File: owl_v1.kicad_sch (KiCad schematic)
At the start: 14 parts, among them SW1 SW_SPDT, U1 STM32F103C8T6, Y1 8MHz, Y2 32k768

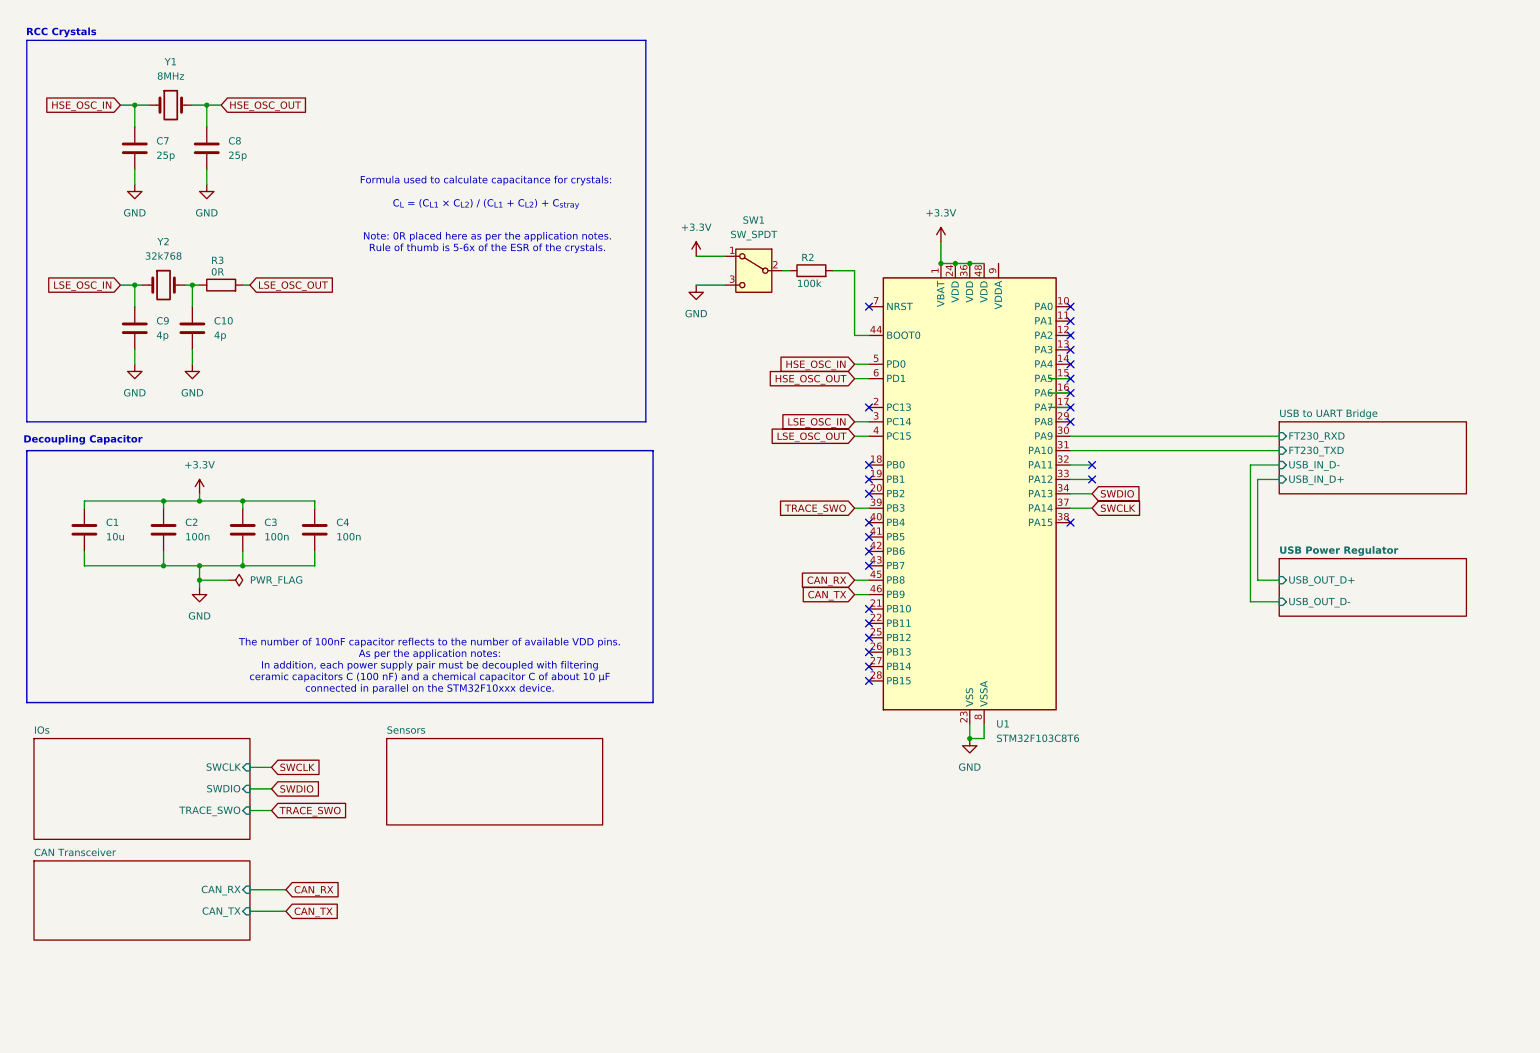
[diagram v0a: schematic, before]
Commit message: [feat] Add breakout for SPI1 for IMU
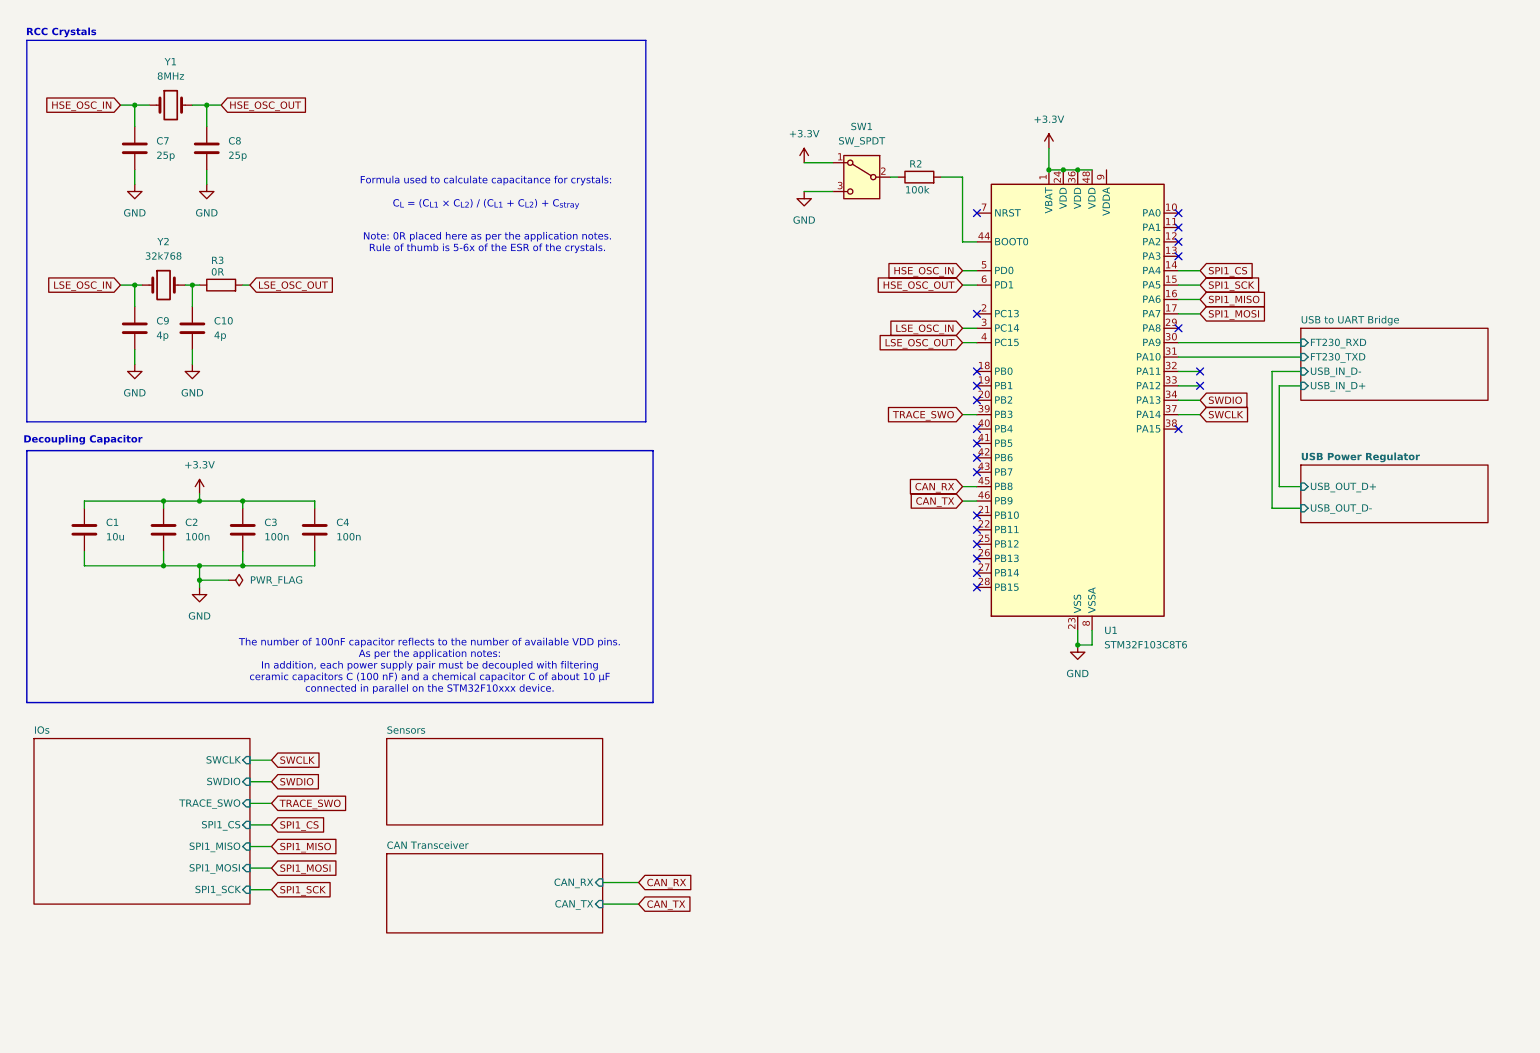
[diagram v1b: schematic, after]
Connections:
- net SPI1_CS: now reaches U1.14 (PA4)
- net SPI1_SCK: now reaches U1.15 (PA5)
- net SPI1_MISO: now reaches U1.16 (PA6)
- net SPI1_MOSI: now reaches U1.17 (PA7)
- no-connect marks 27 -> 23
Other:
- sheet IOs ports: added SPI1_CS, SPI1_MISO, SPI1_MOSI, SPI1_SCK; removed none
- moved on the sheet: R2, SW1, U1

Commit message: [feat] Add analogue filter
The analogue filter has been copied from Phil's lab SimpleTM32
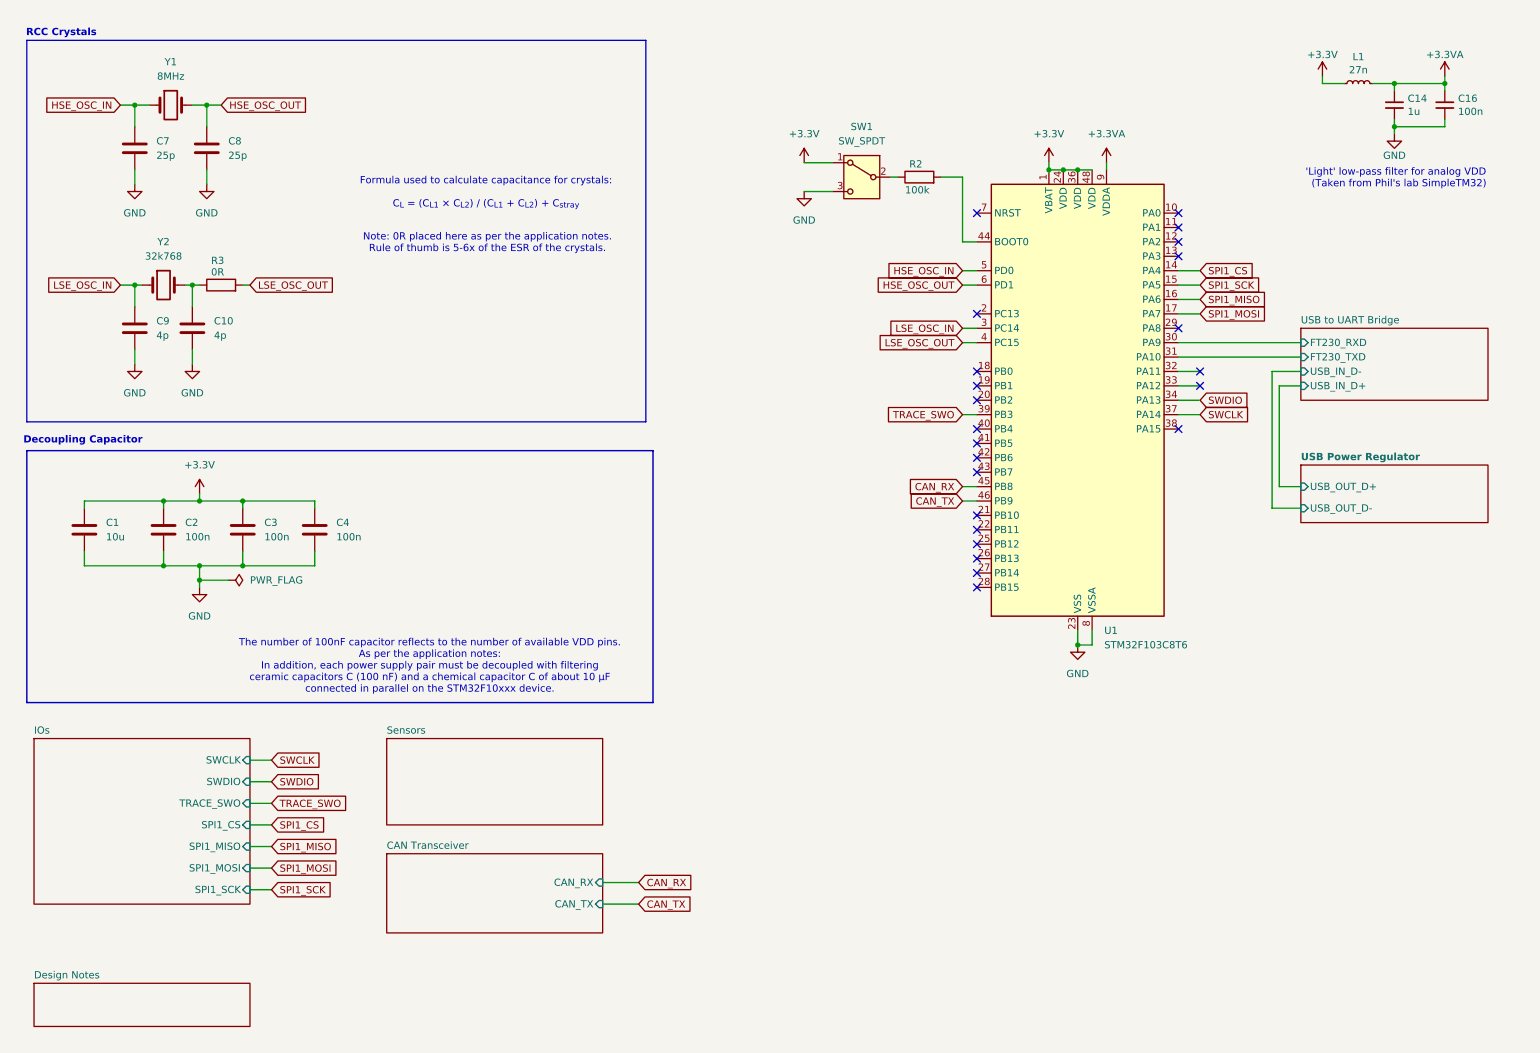
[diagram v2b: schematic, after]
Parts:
- added C14: 1u, Capacitor_SMD:C_0402_1005Metric, symbol Device:C_Small
- added C16: 100n, Capacitor_SMD:C_0402_1005Metric, symbol Device:C_Small
- added L1: 27n, Inductor_SMD:L_0402_1005Metric, symbol Device:L_Small
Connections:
- net +3.3V: now also L1.1
- net GND: now also C14.2, C16.2
- net +3.3VA: now reaches U1.9 (VDDA)
- net +3.3VA: now also C14.1, C16.1, L1.2
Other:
- added sheet Design Notes (design_notes.kicad_sch)
- note added: "'Light' low-pass filter for analog VDD (Taken from Phil's lab SimpleTM32)"

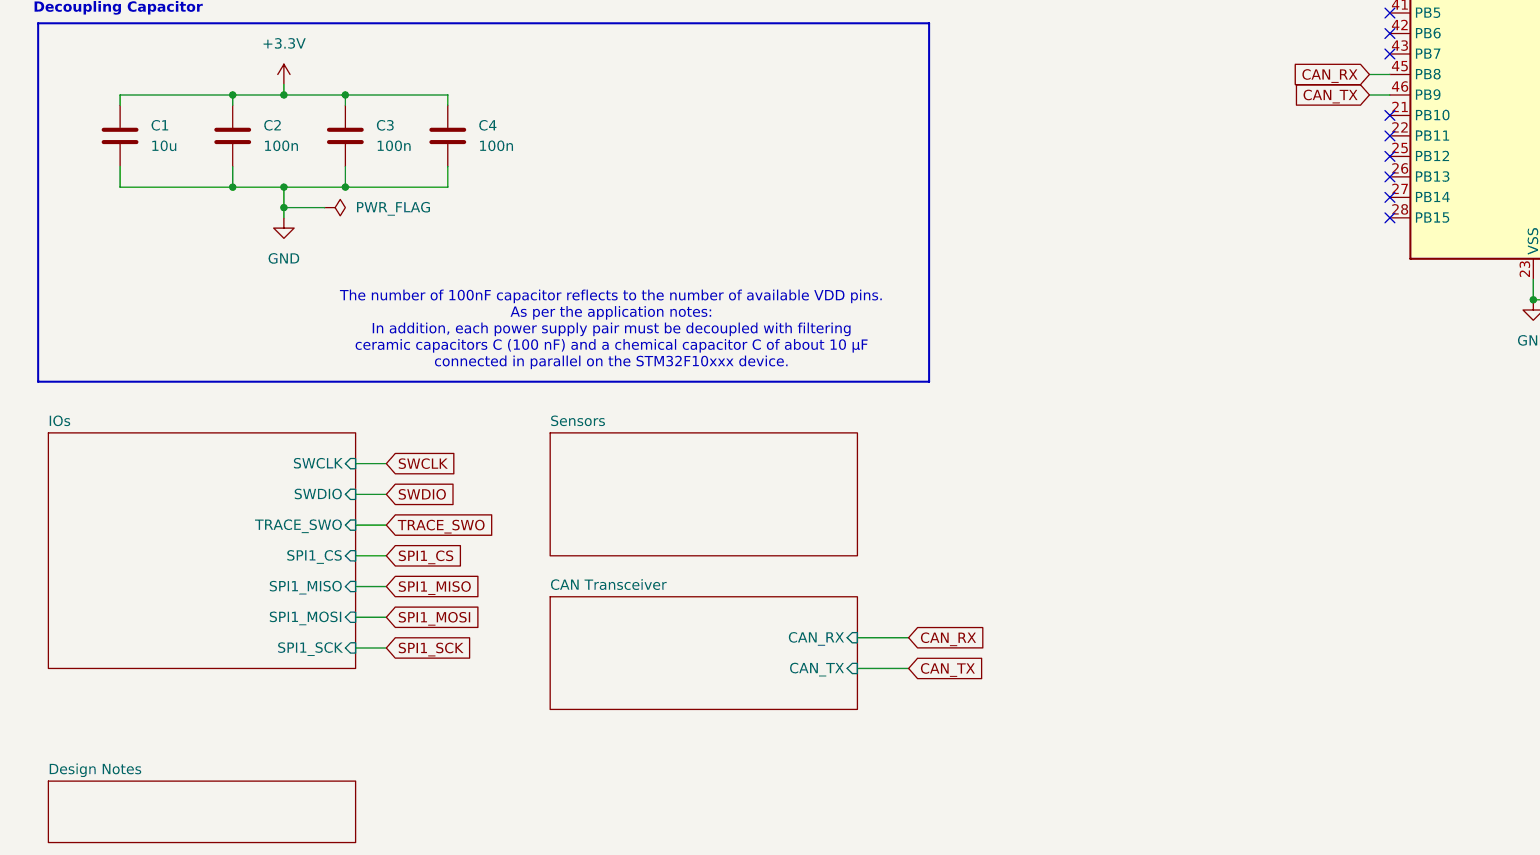
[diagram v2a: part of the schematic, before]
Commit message: [feat] Integrate MicroSD Card into the board with SPI2
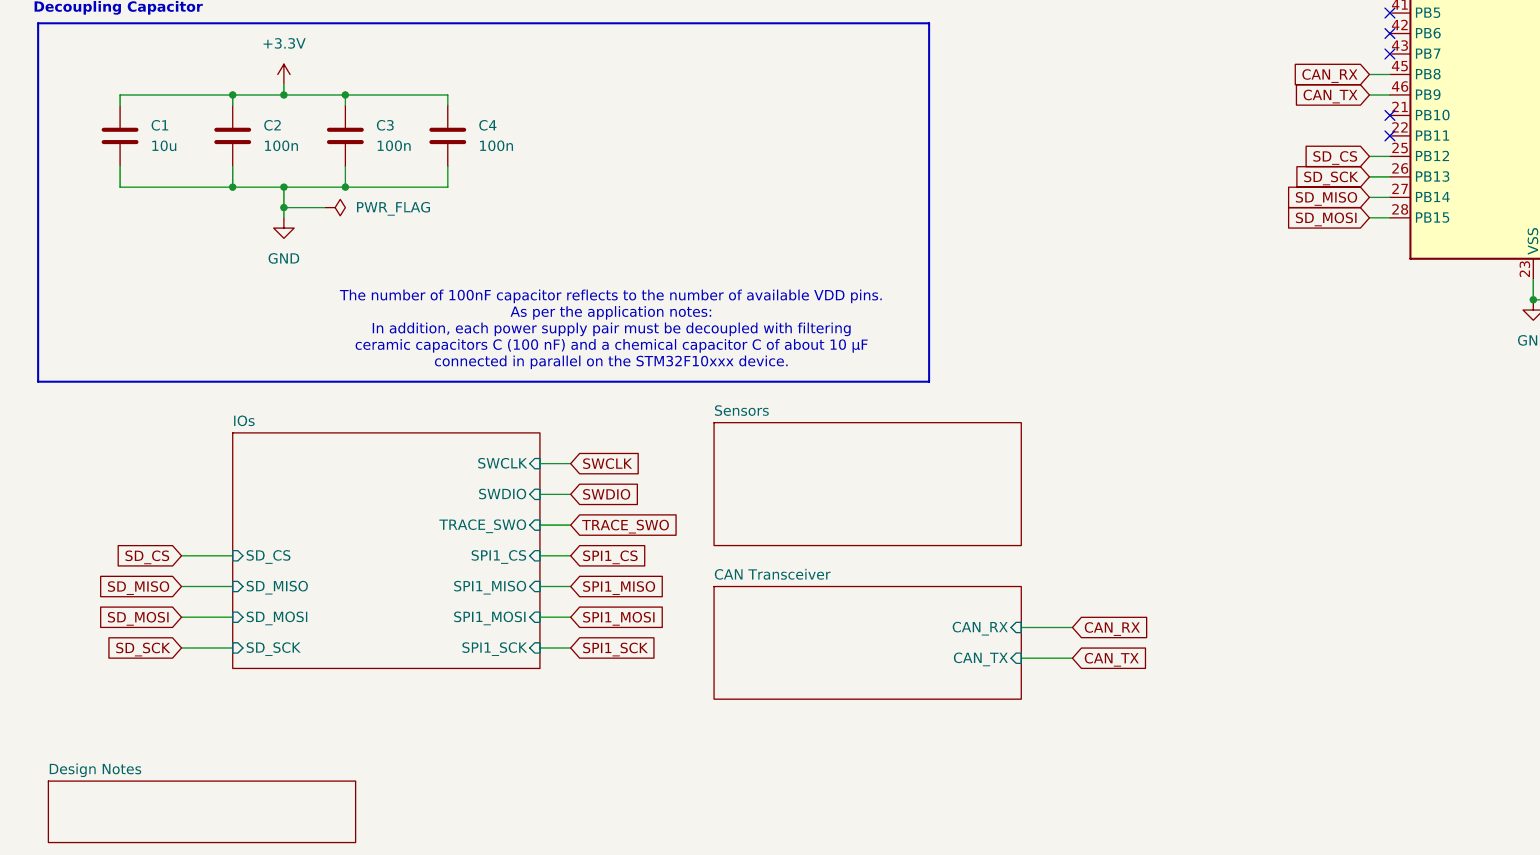
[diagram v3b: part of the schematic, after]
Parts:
- R2: footprint (none) -> Resistor_SMD:R_0603_1608Metric
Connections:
- net SD_CS: now reaches U1.25 (PB12)
- net SD_SCK: now reaches U1.26 (PB13)
- net SD_MISO: now reaches U1.27 (PB14)
- net SD_MOSI: now reaches U1.28 (PB15)
- no-connect marks 23 -> 19
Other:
- sheet IOs ports: added SD_CS, SD_MISO, SD_MOSI, SD_SCK; removed none

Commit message: [feat] Add I2C breakout
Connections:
- net I2C_SCLK: now reaches U1.42 (PB6)
- net I2C_SDA: now reaches U1.43 (PB7)
- no-connect marks 19 -> 17
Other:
- removed sheet Sensors
- sheet IOs ports: added I2C_SCLK, I2C_SDA; removed none
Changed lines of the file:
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@@
 	)
 	(no_connect
-		(at 185.42 96.52)
-	)
-	(no_connect
 		(at 185.42 91.44)
 	)
@@
 	)
 	(no_connect
-		(at 185.42 93.98)
-	)
-	(no_connect
 		(at 185.42 106.68)
 	)
@@
 	(wire
 		(pts
-			(xy 139.7 171.45) (xy 146.05 171.45)
+			(xy 139.7 161.29) (xy 146.05 161.29)
 		)
 		(stroke
@@
 	(wire
 		(pts
+			(xy 182.88 96.52) (xy 185.42 96.52)
+		)
+		(stroke
+			(width 0)
+			(type default)
+		)
+	)
+	(wire
+		(pts
 			(xy 182.88 44.45) (xy 182.88 55.88)
 		)
@@
 	(wire
 		(pts
+			(xy 35.56 154.94) (xy 41.91 154.94)
+		)
+		(stroke
+			(width 0)
+			(type default)
+		)
+	)
+	(wire
+		(pts
 			(xy 27.94 101.6) (xy 27.94 102.87)
 		)
@@
 	(wire
 		(pts
-			(xy 139.7 167.64) (xy 146.05 167.64)
+			(xy 35.56 151.13) (xy 41.91 151.13)
+		)
+		(stroke
+			(width 0)
+			(type default)
+		)
+	)
+	(wire
+		(pts
+			(xy 139.7 157.48) (xy 146.05 157.48)
 		)
 		(stroke
@@
 	(wire
 		(pts
+			(xy 182.88 93.98) (xy 185.42 93.98)
+		)
+		(stroke
+			(width 0)
+			(type default)
+		)
+	)
+	(wire
+		(pts
 			(xy 259.08 36.83) (xy 259.08 35.56)
 		)
@@
 		)
 	)
+	(global_label "I2C_SDA"
+		(shape input)
+		(at 182.88 96.52 180)
+		(fields_autoplaced yes)
+		(effects
+			(font
+				(size 1.27 1.27)
+			)
+			(justify right)
+		)
+		(property "Intersheetrefs" "${INTERSHEET_REFS}"
+			(at 172.2748 96.52 0)
+			(hide yes)
+			(show_name no)
+			(do_not_autoplace no)
+			(effects
+				(font
+					(size 1.27 1.27)
+				)
+				(justify right)
+			)
+		)
+	)
 	(global_label "HSE_OSC_OUT"
 		(shape input)
@@
 		)
 	)
+	(global_label "I2C_SCLK"
+		(shape input)
+		(at 35.56 154.94 180)
+		(fields_autoplaced yes)
+		(effects
+			(font
+				(size 1.27 1.27)
+			)
+			(justify right)
+		)
+		(property "Intersheetrefs" "${INTERSHEET_REFS}"
+			(at 23.7453 154.94 0)
+			(hide yes)
+			(show_name no)
+			(do_not_autoplace no)
+			(effects
+				(font
+					(size 1.27 1.27)
+				)
+				(justify right)
+			)
+		)
+	)
 	(global_label "SD_SCK"
 		(shape input)
@@
 		)
 	)
+	(global_label "I2C_SDA"
+		(shape input)
+		(at 35.56 151.13 180)
+		(fields_autoplaced yes)
+		(effects
+			(font
+				(size 1.27 1.27)
+			)
+			(justify right)
+		)
+		(property "Intersheetrefs" "${INTERSHEET_REFS}"
+			(at 24.9548 151.13 0)
+			(hide yes)
+			(show_name no)
+			(do_not_autoplace no)
+			(effects
+				(font
+					(size 1.27 1.27)
+				)
+				(justify right)
+			)
+		)
+	)
 	(global_label "SD_SCK"
 		(shape input)
@@
 	(global_label "CAN_RX"
 		(shape input)
-		(at 146.05 167.64 0)
+		(at 146.05 157.48 0)
 		(fields_autoplaced yes)
 		(effects
@@
 		)
 		(property "Intersheetrefs" "${INTERSHEET_REFS}"
-			(at 156.1714 167.64 0)
+			(at 156.1714 157.48 0)
 			(hide yes)
 			(show_name no)
@@
 	(global_label "CAN_TX"
 		(shape input)
-		(at 146.05 171.45 0)
+		(at 146.05 161.29 0)
 		(fields_autoplaced yes)
 		(effects
@@
 		)
 		(property "Intersheetrefs" "${INTERSHEET_REFS}"
-			(at 155.869 171.45 0)
+			(at 155.869 161.29 0)
 			(hide yes)
 			(show_name no)
@@
 		)
 	)
+	(global_label "I2C_SCLK"
+		(shape input)
+		(at 182.88 93.98 180)
+		(fields_autoplaced yes)
+		(effects
+			(font
+				(size 1.27 1.27)
+			)
+			(justify right)
+		)
+		(property "Intersheetrefs" "${INTERSHEET_REFS}"
+			(at 171.0653 93.98 0)
+			(hide yes)
+			(show_name no)
+			(do_not_autoplace no)
+			(effects
+				(font
+					(size 1.27 1.27)
+				)
+				(justify right)
+			)
+		)
+	)
 	(symbol
 		(lib_id "Device:C")
@@
 	)
 	(sheet
-		(at 101.6 162.56)
+		(at 101.6 152.4)
 		(size 38.1 13.97)
 		(exclude_from_sim no)
@@
 		)
 		(property "Sheetname" "CAN Transceiver"
-			(at 101.6 161.8484 0)
+			(at 101.6 151.6884 0)
 			(show_name no)
 			(do_not_autoplace no)
@@
 		)
 		(property "Sheetfile" "can_controller.kicad_sch"
-			(at 101.6 177.1146 0)
+			(at 101.6 166.9546 0)
 			(hide yes)
 			(show_name no)
@@
 		)
 		(pin "CAN_RX" input
-			(at 139.7 167.64 0)
+			(at 139.7 157.48 0)
 			(effects
 				(font
@@
 		)
 		(pin "CAN_TX" input
-			(at 139.7 171.45 0)
+			(at 139.7 161.29 0)
 			(effects
 				(font
@@
 	)
 	(sheet
-		(at 19.05 186.69)
+		(at 69.85 182.88)
 		(size 38.1 7.62)
 		(exclude_from_sim no)
@@
 		)
 		(property "Sheetname" "Design Notes"
-			(at 19.05 185.9784 0)
+			(at 69.85 182.1684 0)
 			(show_name no)
 			(do_not_autoplace no)
@@
 		)
 		(property "Sheetfile" "design_notes.kicad_sch"
-			(at 19.05 194.8946 0)
+			(at 69.85 191.0846 0)
 			(hide yes)
 			(show_name no)
@@
 	(sheet
 		(at 41.91 143.51)
-		(size 38.1 29.21)
+		(size 38.1 30.48)
 		(exclude_from_sim no)
 		(in_bom yes)
@@
 		)
 		(property "Sheetfile" "GPIOs.kicad_sch"
-			(at 41.91 173.3046 0)
+			(at 41.91 174.5746 0)
 			(hide yes)
 			(show_name no)
@@
 			)
 		)
+		(pin "I2C_SCLK" input
+			(at 41.91 154.94 180)
+			(effects
+				(font
+					(size 1.27 1.27)
+				)
+				(justify left)
+			)
+		)
+		(pin "I2C_SDA" input
+			(at 41.91 151.13 180)
+			(effects
+				(font
+					(size 1.27 1.27)
+				)
+				(justify left)
+			)
+		)
 		(instances
 			(project "owl_v1"
@@
 				)
 			)
-		)
-	)
-	(sheet
-		(at 101.6 142.24)
-		(size 38.1 15.24)
-		(exclude_from_sim no)
-		(in_bom yes)
-		(on_board yes)
-		(dnp no)
-		(fields_autoplaced yes)
-		(stroke
-			(width 0.1524)
-			(type solid)
-		)
-		(fill
-			(color 0 0 0 0)
-		)
-		(property "Sheetname" "Sensors"
-			(at 101.6 141.5284 0)
-			(show_name no)
-			(do_not_autoplace no)
-			(effects
-				(font
-					(size 1.27 1.27)
-				)
-				(justify left bottom)
-			)
-		)
-		(property "Sheetfile" "sensors.kicad_sch"
-			(at 101.6 158.0646 0)
-			(hide yes)
-			(show_name no)
-			(do_not_autoplace no)
-			(effects
-				(font
-					(size 1.27 1.27)
-				)
-				(justify left top)
-			)
-		)
-		(instances
-			(project "owl_v1"
-				(path "/c1d8d3e2-84ea-437a-bbb1-a2e651deb7ac"
-					(page "5")
-				)
-			)
